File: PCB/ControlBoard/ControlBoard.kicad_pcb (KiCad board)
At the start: 4 copper layers, 98 x 58 mm, 74 parts, among them J1 ICSP, J10 BUSPWR, J3 Bus, J4 Submodule A, J5 Submodule B, J6 Submodule C, J7 uSD, J8 ARGB, J9 Indicator, Q1 Q_PMOS_GSD, SW1 Boot, U1 PIC18F57Q84, U2 MCP2562-E-SN, U3 74LVC125, U4 SN74AHCT1G125, U5 TPS629210, U6 TPS629210, U7 CM1293A‐04SO

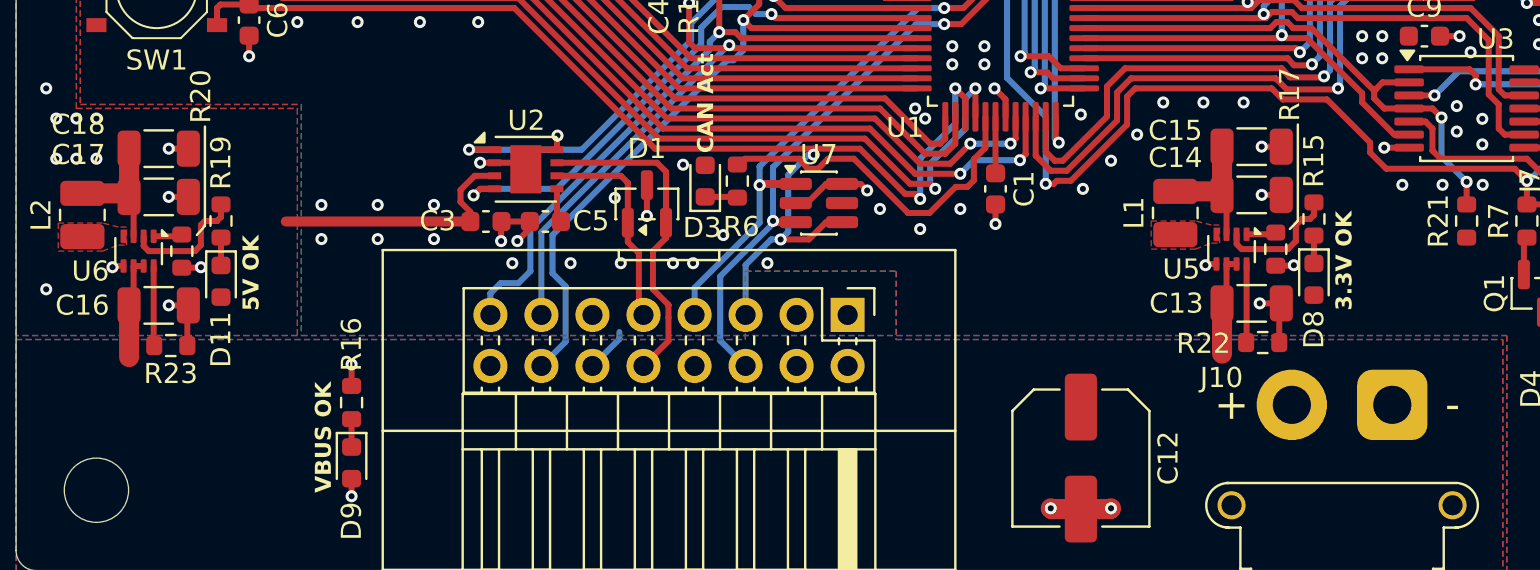
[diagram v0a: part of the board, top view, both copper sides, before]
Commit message: Fix up power LEDs on regulators.
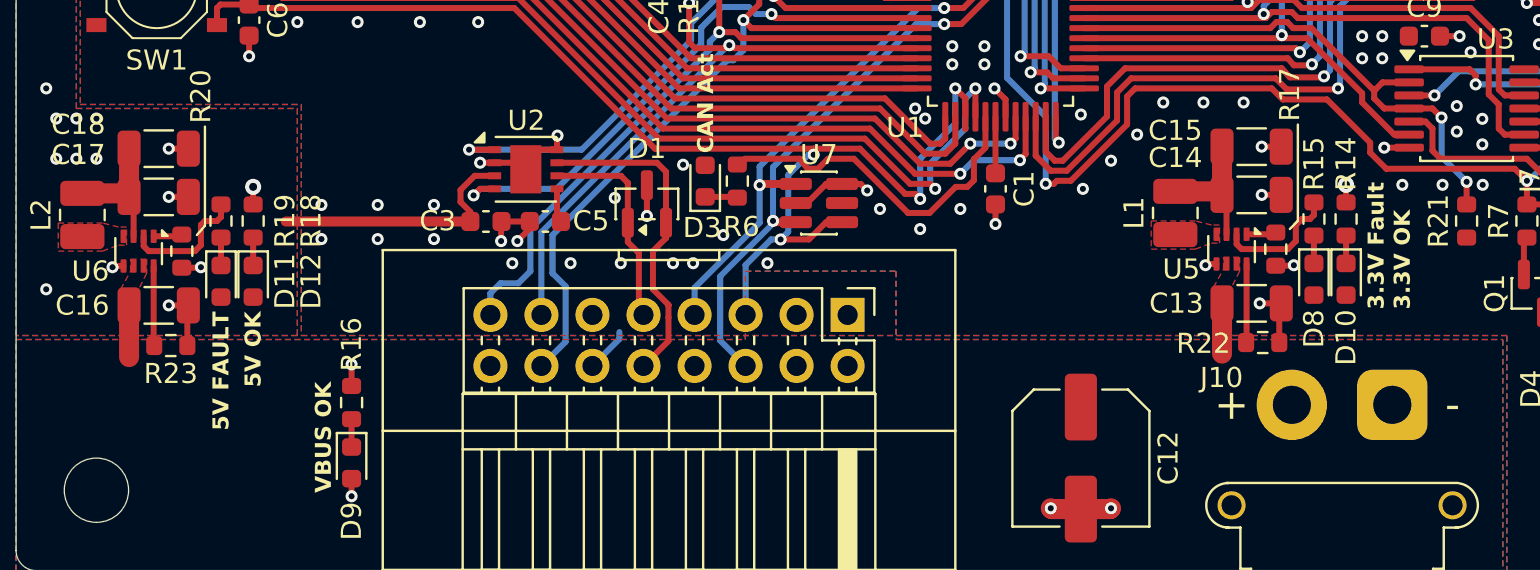
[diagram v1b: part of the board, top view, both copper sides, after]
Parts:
- added D10: 3.3V OK, LED_SMD:LED_0603_1608Metric, F.Cu at (87.2, 64.5)
- added D12: 5V OK, LED_SMD:LED_0603_1608Metric, F.Cu at (32.8, 64.6)
- added R14: 10k, Resistor_SMD:R_0603_1608Metric, F.Cu at (87.2, 61.5)
- added R18: 10k, Resistor_SMD:R_0603_1608Metric, F.Cu at (32.8, 61.6)
- D11: value 5V OK -> 5V Fault
- D8: value 3.3V OK -> 3.3V Fault
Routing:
- net VDD: track 11.4 -> 6.89 mm
- net GND: track 61.4 -> 63.2 mm, vias 41 -> 43
- net Net-(D12-K): track 0.00 -> 1.39 mm
- net Net-(D10-K): track 0.00 -> 1.39 mm
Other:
- board text added: "3.3V Fault"
- board text added: "5V FAULT"

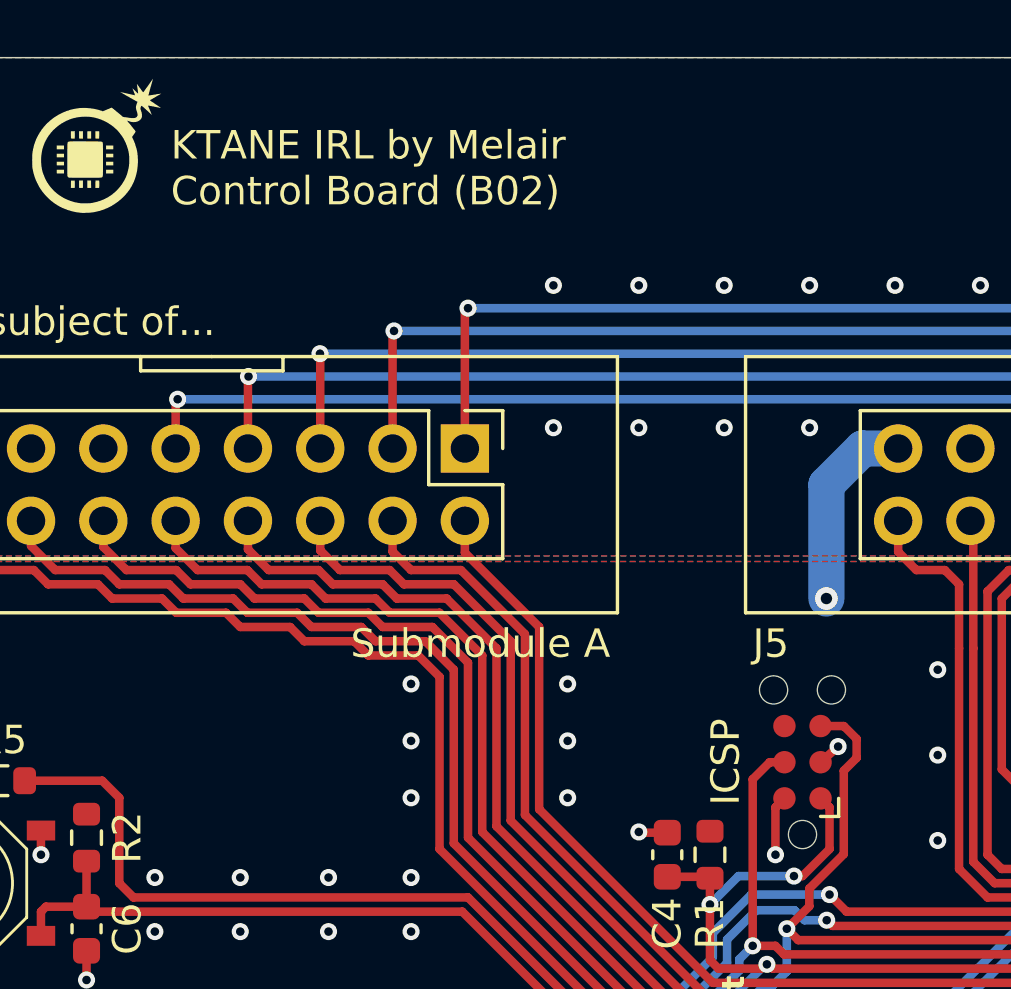
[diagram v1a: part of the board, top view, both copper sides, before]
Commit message: Include all corrections, mint new gerbers. Update some to KiCad 10.
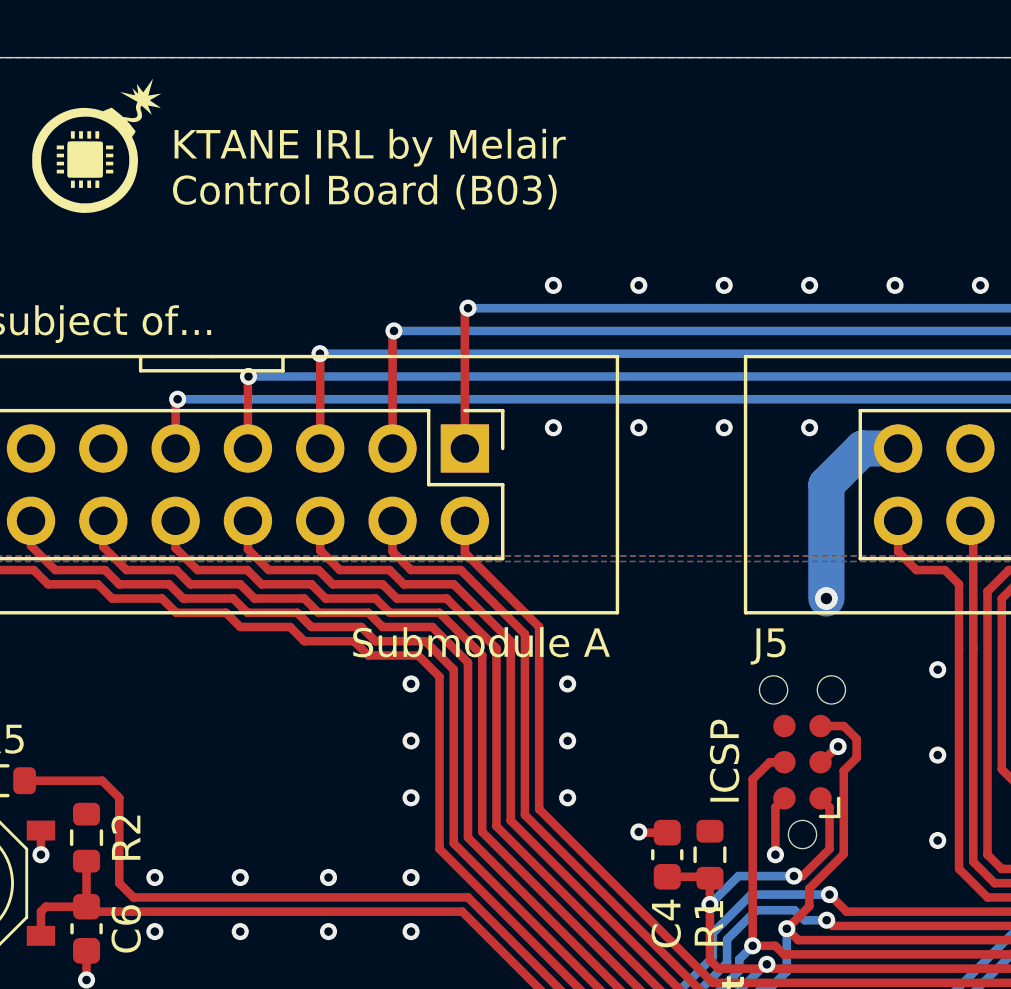
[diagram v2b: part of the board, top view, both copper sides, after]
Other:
- board text added: "KTANE IRL by Melair Control Board (B03)"
- board text removed: "KTANE IRL by Melair Control Board (B02)"

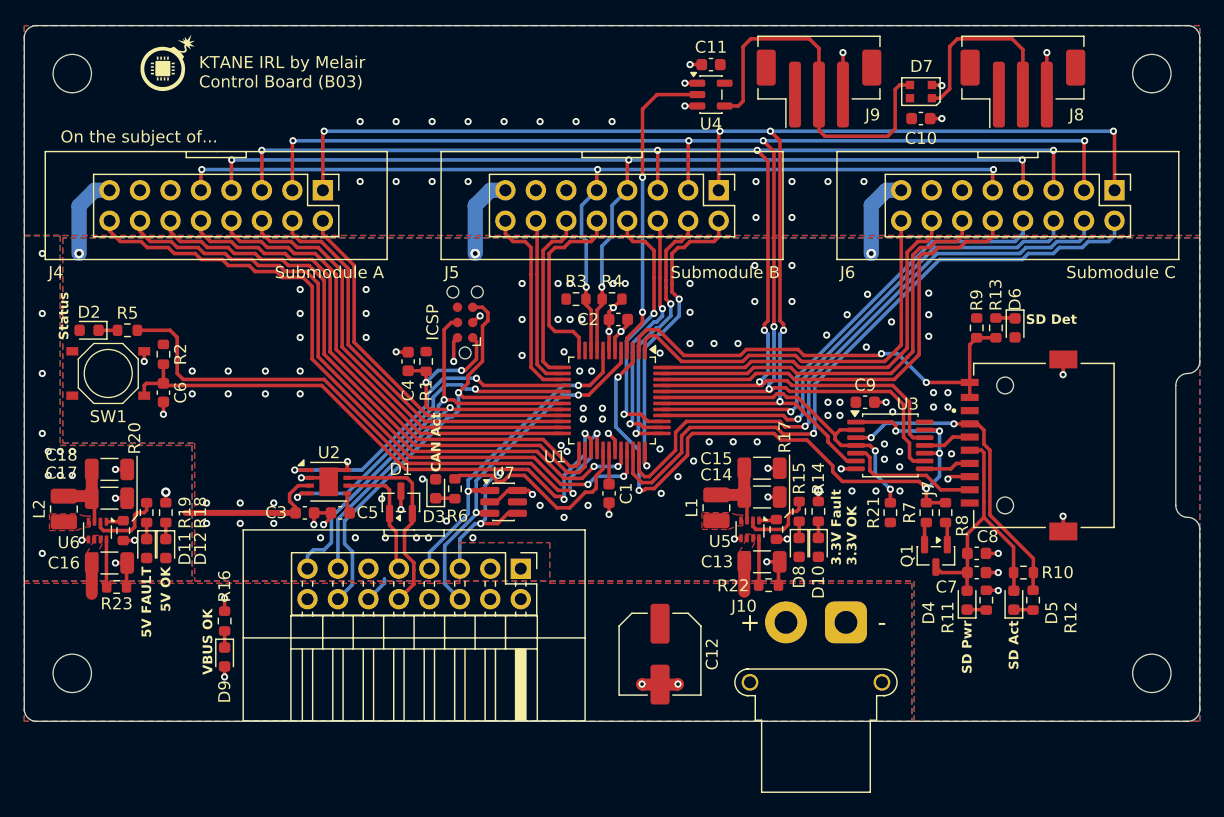
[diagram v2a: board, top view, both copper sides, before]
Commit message: feat: Rework ControlBoard to use an STM32H562VGT6.
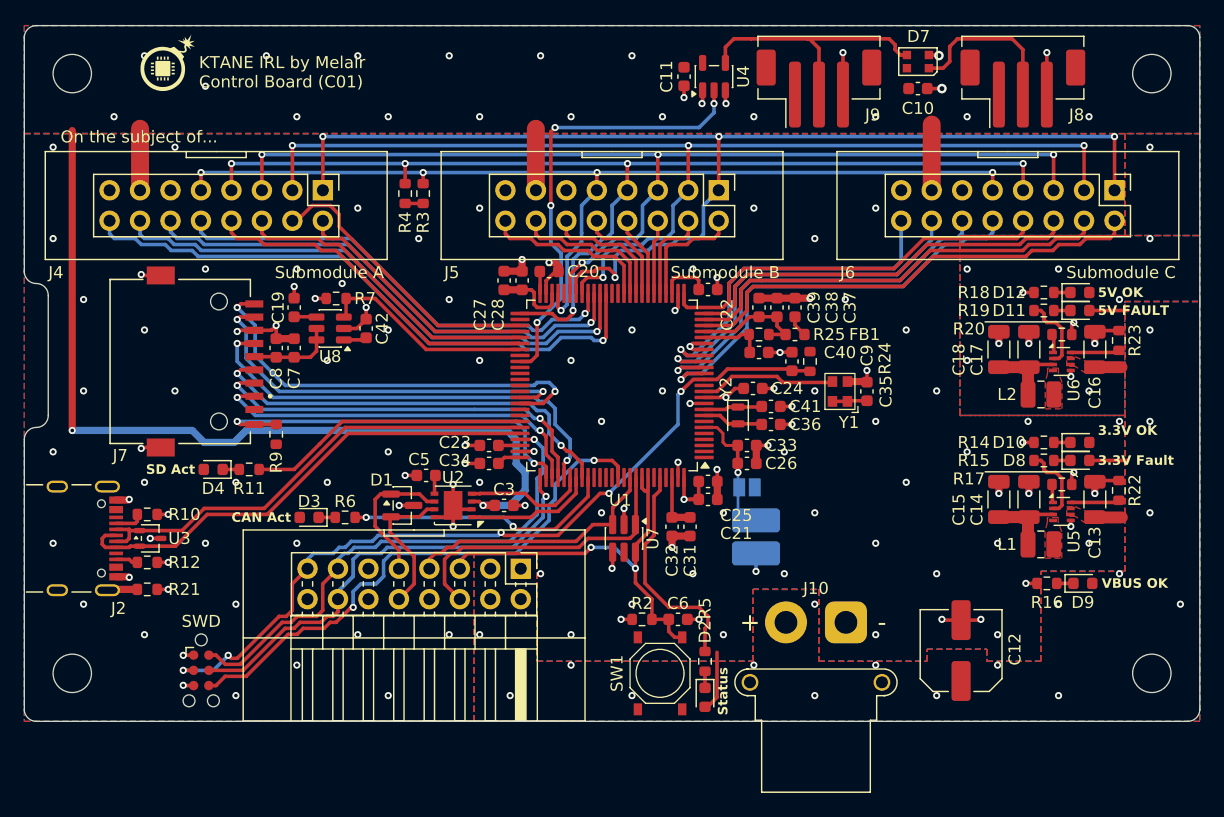
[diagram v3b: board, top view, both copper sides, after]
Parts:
- removed C1, C2, C4: 0.1μF, Capacitor_SMD:C_0603_1608Metric
- removed D5: SD Act, LED_SMD:LED_0603_1608Metric
- removed D6: SD Present, LED_SMD:LED_0603_1608Metric
- removed Q1: Q_PMOS_GSD, Package_TO_SOT_SMD:SOT-23
- removed R1: 10k, Resistor_SMD:R_0603_1608Metric
- removed R13: 1000, Resistor_SMD:R_0603_1608Metric
- removed R8: 120, Resistor_SMD:R_0603_1608Metric
- added C19: 470nF, Capacitor_SMD:C_0603_1608Metric, F.Cu at (43.5, 44.5)
- added C20: 0.1uF, Capacitor_SMD:C_0603_1608Metric, F.Cu at (64.8, 41.5)
- added C21: 0.1μF, Capacitor_SMD:C_0603_1608Metric, F.Cu at (78.0, 60.5)
- added C22: 0.1μF, Capacitor_SMD:C_0603_1608Metric, F.Cu at (78.0, 43.0)
- added C23: 0.1μF, Capacitor_SMD:C_0603_1608Metric, F.Cu at (59.8, 56.0)
- added C24: 0.1μF, Capacitor_SMD:C_0603_1608Metric, F.Cu at (81.8, 51.2)
- added C25: 4.7uF, Capacitor_SMD:C_0603_1608Metric, F.Cu at (78.0, 59.0)
- added C26: 0.1uF, Capacitor_SMD:C_0603_1608Metric, F.Cu at (81.2, 57.5)
- added C27: 2.2uF, Capacitor_SMD:C_0603_1608Metric, F.Cu at (61.0, 42.2)
- added C28: 2.2uF, Capacitor_SMD:C_0603_1608Metric, F.Cu at (62.5, 42.2)
- added C31: 2.2uF, Capacitor_SMD:C_0603_1608Metric, F.Cu at (76.5, 62.8)
- added C32: 2.2uF, Capacitor_SMD:C_0603_1608Metric, F.Cu at (75.0, 62.8)
- added C33: 1μF, Capacitor_SMD:C_0603_1608Metric, F.Cu at (81.2, 56.0)
- added C34: 0.1uF, Capacitor_SMD:C_0603_1608Metric, F.Cu at (59.8, 57.5)
- added C35: 0.1μF, Capacitor_SMD:C_0603_1608Metric, F.Cu at (91.2, 51.5)
- added C36: 8pF, Capacitor_SMD:C_0603_1608Metric, F.Cu at (83.2, 54.2)
- added C37: 1μF, Capacitor_SMD:C_0603_1608Metric, F.Cu at (85.2, 44.5)
- added C38: 1μF, Capacitor_SMD:C_0603_1608Metric, F.Cu at (83.8, 44.5)
- added C39: 0.1uF, Capacitor_SMD:C_0603_1608Metric, F.Cu at (82.2, 44.5)
- added C40: 0.1μF, Capacitor_SMD:C_0603_1608Metric, F.Cu at (82.2, 48.2)
- added C41: 8pF, Capacitor_SMD:C_0603_1608Metric, F.Cu at (83.2, 52.8)
- added C42: 0.1μF, Capacitor_SMD:C_0603_1608Metric, F.Cu at (49.5, 46.2)
- added FB1: 600, Inductor_SMD:L_0603_1608Metric, F.Cu at (85.2, 46.8)
- added J11: BATT +, KTANE:Pad4x2, B.Cu at (82.0, 62.2)
- added J12: BATT -, KTANE:Pad4x2, B.Cu at (82.0, 65.0)
- added J2: USB, KTANE:SAMESKY_UJ20-C-H-G-SMT-1A-P16-TR, F.Cu at (23.8, 63.8)
- added JP1: NoBatt, Jumper:SolderJumper-2_P1.3mm_Open_Pad1.0x1.5mm, B.Cu at (81.2, 59.5)
- added R24: 10k, Resistor_SMD:R_0603_1608Metric, F.Cu at (86.5, 49.0)
- added R25: 47, Resistor_SMD:R_0603_1608Metric, F.Cu at (82.2, 46.8)
- added U8: TPS22918, Package_TO_SOT_SMD:SOT-23-6, F.Cu at (46.5, 46.2)
- added Y1: XO22C3EREHX50M000, KTANE:Oscillator_SMD-Vishay_X022C_2.5mmx2.0mm, F.Cu at (89.0, 51.5)
- added Y2: 32.768k, Crystal:Crystal_SMD_2012-2Pin_2.0x1.2mm, F.Cu at (80.5, 53.5)
- D4: value SD Pwr -> SD Act
- H1, H2, H3, H4: footprint MountingHole:MountingHole_3.2mm_M3 -> KTANE:MountingHole_3.2mm_M3_NoCopper
- J1: value ICSP -> SWD
- R10: value 10k -> 5.1k
- R12: value 1000 -> 5.1k
- R14, R18: value 10k -> 1000
- R15, R19: value 1000 -> 10k
- R21: value 10k -> 1M
- U1: value PIC18F57Q84 -> STM32H562VGT6; footprint Package_QFP:TQFP-48_7x7mm_P0.5mm -> Package_QFP:LQFP-100_14x14mm_P0.5mm
- U3: value 74LVC125 -> TPD2E2U06DCK; footprint Package_SO:TSSOP-14_4.4x5mm_P0.65mm -> Package_TO_SOT_SMD:SOT-323_SC-70
- moved R23 86.0 mm to (112.2, 47.2), turned to 90 degrees
- moved C16 84.1 mm to (110.2, 48.0), turned to 90 degrees
- moved L2 82.0 mm to (105.8, 51.8), turned to 180 degrees
- moved U6 81.6 mm to (107.5, 49.0), turned to 0 degrees
- moved D11 80.3 mm to (109.0, 44.8), turned to 0 degrees
- moved R20 79.9 mm to (107.5, 46.8), turned to 0 degrees
- moved D12 79.1 mm to (109.0, 43.2), turned to 0 degrees
- moved C17 77.6 mm to (104.8, 48.0), turned to 90 degrees
- moved R19 76.7 mm to (106.0, 44.8), turned to 180 degrees
- moved R18 75.5 mm to (106.0, 43.2), turned to 180 degrees
- moved C18 74.8 mm to (102.2, 48.0), turned to 90 degrees
- moved R12 73.9 mm to (31.2, 65.8), turned to 180 degrees
- moved R10 73.2 mm to (31.2, 61.8)
- moved J7 72.3 mm to (34.0, 49.0), turned to -90 degrees
- moved D9 71.8 mm to (109.2, 67.5), turned to 0 degrees
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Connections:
- C7 pad 1: Net-(D4-A) -> Net-(J7-VDD)
- C8 pad 1: Net-(D4-A) -> Net-(J7-VDD)
- C9 pad 1: +3.3V -> ~{RESET}
- D11 pad 2: +5V -> VDD
- D4 pad 2: Net-(D4-A) -> +3.3V
- D8 pad 2: +3.3V -> VDD
- J1 pad 1: ~{MCLR} -> +3.3V
- J1 pad 2: +3.3V -> SWDIO
- J1 pad 3: GND -> ~{RESET}
- J1 pad 4: ICSPDAT -> SWCLK
- J1 pad 5: ICSPCLK -> GND
- J1 pad 6: unconnected-(J1-Pin_6-Pad6) -> SWO
- J3 pad 13: ~{MCLR} -> SWDIO
- J3 pad 14: ICSPCLK -> SWCLK
- J3 pad 15: ICSPDAT -> ~{RESET}
- J4 pad 10: /A3 -> /A4
- J4 pad 12: /A2 -> /A5
- J4 pad 14: /A1 -> /A6
- J4 pad 16: /A0 -> /A7
- J4 pad 2: /A7 -> /A0
- J4 pad 4: /A6 -> /A1
- J4 pad 6: /A5 -> /A2
- J4 pad 8: /A4 -> /A3
- J5 pad 10: /B3 -> /B4
- J5 pad 12: /B2 -> /B5
- J5 pad 14: /B1 -> /B6
- J5 pad 16: /B0 -> /B7
- J5 pad 2: /B7 -> /B0
- J5 pad 4: /B6 -> /B1
- J5 pad 6: /B5 -> /B2
- J5 pad 8: /B4 -> /B3
- J6 pad 10: /C3 -> /C4
- J6 pad 12: /C2 -> /C5
- J6 pad 14: /C1 -> /C6
- J6 pad 16: /C0 -> /C7
- J6 pad 2: /C7 -> /C0
- J6 pad 4: /C6 -> /C1
- J6 pad 6: /C5 -> /C2
- J6 pad 8: /C4 -> /C3
- J7 pad CD: SD-PRESENT -> ~{SD-PRESENT}
- J7 pad P1: unconnected-(J7-DAT2-PadP1) -> SD-DAT2
- J7 pad P2: ~{BUF-CS} -> SD-DAT3
- J7 pad P3: SD-COPI -> SD-CMD
- J7 pad P4: Net-(D4-A) -> Net-(J7-VDD)
- J7 pad P7: SD-CIPO -> SD-DAT0
- J7 pad P8: unconnected-(J7-DAT1-PadP8) -> SD-DAT1
- J7 pad WP: SD-PRESENT -> unconnected-(J7-PadWP)
- R10 pad 1: ~{BUF-CS} -> GND
- R10 pad 2: Net-(D4-A) -> Net-(J2-CC1)
- R11 pad 2: GND -> SD-ACT
- R12 pad 1: Net-(D5-K) -> GND
- R12 pad 2: ~{BUF-CS} -> Net-(J2-CC2)
- R2 pad 1: +3.3V -> BOOT
- R2 pad 2: BOOT -> GND
- R21 pad 1: ~{SD-CS} -> Net-(J2-SHIELD-PadSH1)
- R21 pad 2: +3.3V -> GND
- R7 pad 1: ~{SD-PWR} -> GND
- R7 pad 2: +3.3V -> SD-PWR
- R9 pad 1: SD-PRESENT -> ~{SD-PRESENT}
- SW1 pad 3: GND -> +3.3V
- U1 pad 1: /C0 -> unconnected-(U1-PE2-Pad1)
- U1 pad 10: I2C-CLK -> GND
- U1 pad 11: unconnected-(U1-RB3-Pad11) -> +3.3V
- U1 pad 12: /B3 -> Net-(U1-PH0)
- U1 pad 13: /B2 -> unconnected-(U1-PH1-Pad13)
- U1 pad 14: /B1 -> ~{RESET}
- U1 pad 15: /B0 -> /C4
- U1 pad 16: CANTX -> /C5
- U1 pad 17: CANRX -> /C6
- U1 pad 18: ICSPCLK -> /C7
- U1 pad 19: ICSPDAT -> GND
- U1 pad 2: SD-PRESENT -> unconnected-(U1-PE3-Pad2)
- U1 pad 20: ~{MCLR} -> GND
- U1 pad 21: /A7 -> Net-(U1-VREF+)
- U1 pad 22: /A6 -> +3.3VA
- U1 pad 23: /A5 -> /C0
- U1 pad 24: /A4 -> /C1
- U1 pad 25: /A3 -> /C2
- U1 pad 26: /A2 -> /C3
- U1 pad 27: BOOT -> GND
- U1 pad 28: STATUS-LED -> +3.3V
- U1 pad 29: CAN-ACT-LED -> /B0
- U1 pad 3: ~{SD-PWR} -> unconnected-(U1-PE4-Pad3)
- U1 pad 30: +3.3V -> /B1
- U1 pad 31: GND -> /B2
- U1 pad 32: /A1 -> /B3
- U1 pad 33: /A0 -> /B4
- U1 pad 34: /C7 -> /B5
- U1 pad 35: /C6 -> /B6
- U1 pad 37: /B6 -> unconnected-(U1-PB2-Pad37)
- U1 pad 38: /B5 -> unconnected-(U1-PE7-Pad38)
- U1 pad 39: /B4 -> /A7
- U1 pad 4: ARGB -> unconnected-(U1-PE5-Pad4)
- U1 pad 40: /C5 -> /A6
- U1 pad 41: /C4 -> /A5
- U1 pad 42: SPI-CIPO -> /A4
- U1 pad 43: ~{SD-CS} -> SPI-CLK
- U1 pad 44: SPI-CLK -> SPI-CIPO
- U1 pad 46: /C3 -> unconnected-(U1-PE15-Pad46)
- U1 pad 47: /C2 -> I2C-CLK
- U1 pad 48: /C1 -> Net-(C27-Pad1)
- U1 pad 5: UART-RX -> unconnected-(U1-PE6-Pad5)
- U1 pad 6: GND -> +BATT
- U1 pad 7: +3.3V -> unconnected-(U1-PC13-Pad7)
- U1 pad 8: UART-TX -> Net-(U1-PC14)
- U1 pad 9: I2C-DAT -> Net-(U1-PC15)
- U3 pad 1: ~{SD-PWR} -> USB-DM
- U3 pad 2: ~{SD-CS} -> USB-DP
- U3 pad 3: ~{BUF-CS} -> GND
- U7 pad 1: UART-TX -> UART-RX
- U7 pad 3: UART-RX -> UART-TX
- U7 pad 4: BOOT -> GND
- U7 pad 6: GND -> BOOT
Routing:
- net +5V: track 19.8 -> 96.4 mm, vias 29 -> 26
- net ~{RESET}: track 0.00 -> 67.2 mm, vias 0 -> 5
- net ~{SD-PWR}: track 61.0 -> 0.00 mm, vias 6 -> 0
- net SWO: track 0.00 -> 46.0 mm, vias 0 -> 2
- net GND: track 63.2 -> 106.6 mm, vias 43 -> 65
- net SWDIO: track 0.00 -> 42.6 mm, vias 0 -> 1
- net USB-DP: track 0.00 -> 40.6 mm
- net ~{MCLR}: track 40.1 -> 0.00 mm, vias 3 -> 0
- net ICSPCLK: track 40.0 -> 0.00 mm, vias 1 -> 0
- net USB-DM: track 0.00 -> 39.2 mm
- net SWCLK: track 0.00 -> 38.8 mm, vias 0 -> 1
- net SD-PRESENT: track 38.1 -> 0.00 mm, vias 2 -> 0
- net /A0: track 58.5 -> 20.9 mm, vias 2 -> 0
- net SD-DAT1: track 0.00 -> 37.0 mm, vias 0 -> 2
- net ICSPDAT: track 36.5 -> 0.00 mm, vias 1 -> 0
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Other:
- outline, holes or cut-outs redrawn
- board text added: "KTANE IRL by Melair Control Board (C01)"
- board text added: "{dblquote}Common misconception that; that fun is relaxing. If it is, you're not doing it right.{dblquote} Iain M. Banks, The Player of Games"
- board text removed: "KTANE IRL by Melair Control Board (B03)"
- board text removed: "SD Det"
- board text removed: "SD Pwr"

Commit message: fix: Adjust labels on regulator.
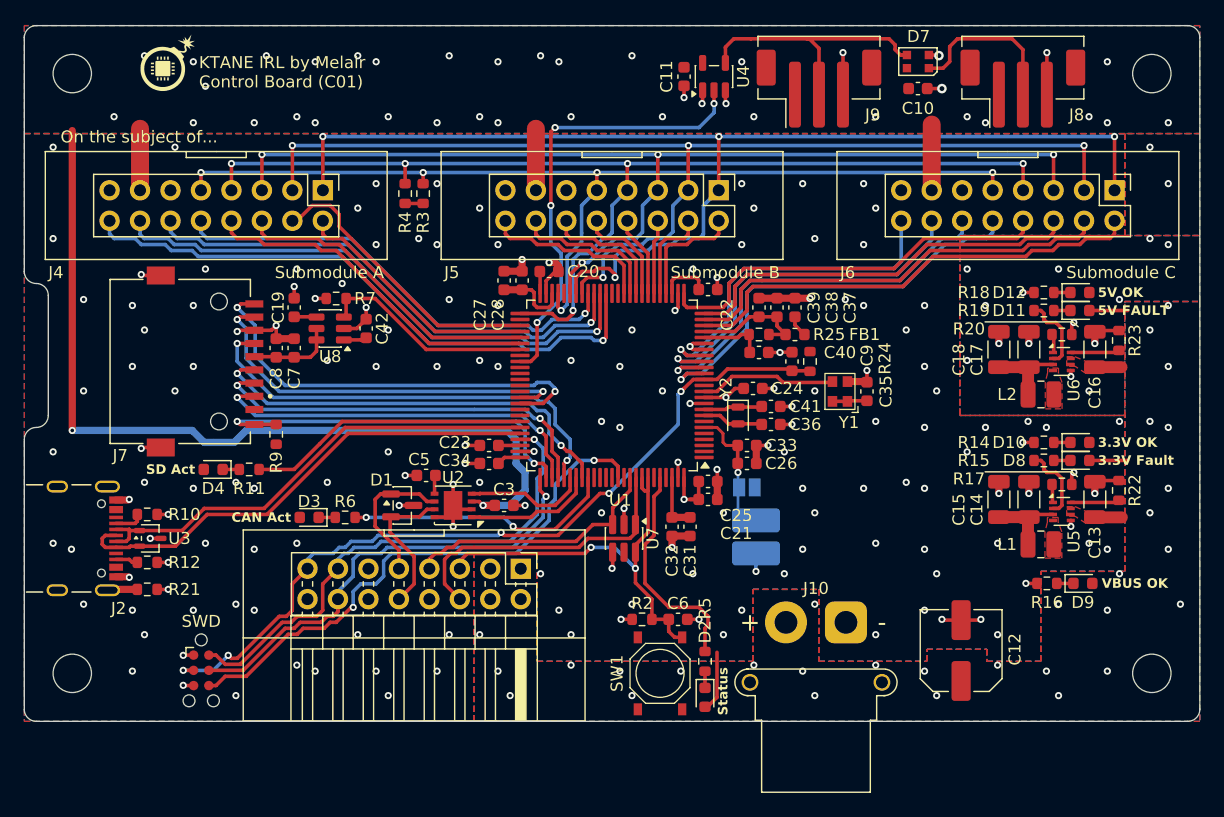
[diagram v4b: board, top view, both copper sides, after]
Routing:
- net GND: vias 65 -> 142
